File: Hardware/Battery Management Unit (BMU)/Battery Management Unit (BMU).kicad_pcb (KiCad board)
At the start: 4 copper layers, 105 x 65.5 mm, 93 parts, among them IC1 STM32C092RCT6, J1 HIGH SIDE, J10 SHUNT, J11 ALERT, J12 CAN, J13 Conn_ST_STDC14, J2 LOW SIDE, J3 POWER, J4 GPIO, J5 GND, J6 5V, J7 3V3, J8 FAULT, J9 I2C, Q1 DMP3099L, SW1 Power Switch, SW2 RESET Switch, T1 CEP99-102, T2 CEP99-102, U1 OKI-78SR-5_1.5-W36-C, U2 TLV75533PDBV, U3 PESD5V0L2BT, U4 BQ79600PWRQ1, U5 PESD5V0L2BT, U6 MCP2562FDT-H_SN

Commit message: Both boards are now fully completed: the BMU and CMU.
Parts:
- moved TP8 0.56 mm to (170.5, 87.8)
- moved TP14 0.28 mm to (151.5, 130.8)
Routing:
- net /BMU-COM Bridge/MISO/TX: track 29.9 -> 30.8 mm
- net /BMU-MCU/ALERT_SHUNT: track 49.3 -> 50.1 mm
- net /BMU-COM Bridge/FAULT_N: track 30.3 -> 29.6 mm
- net Net-(U4-BAT): track 16.2 -> 16.8 mm
- net /J4_CANL: track 24.7 -> 25.3 mm
- net /BMU-COM Bridge/MOSI/RX: track 37.4 -> 38.0 mm
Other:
- board text added: "VIKING MOTOR SPORTS (VMS) Battery Management Unit (BMU) 2026.4 Capstone TEAM-12"
- board text removed: "VIKING MOTOR SPORTS (VMS) BATTERY MANAGEMENT UNIT (BMU) 2026.4 Capstone TEAM-12"

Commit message: update layout
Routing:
- net +5V: vias 5 -> 4
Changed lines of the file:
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@@
-	)
-	(via
-		(at 171.5 102.5)
-		(size 0.6)
-		(drill 0.3)
-		(layers "F.Cu" "B.Cu")
-		(net "+5V")
 	)
 	(via

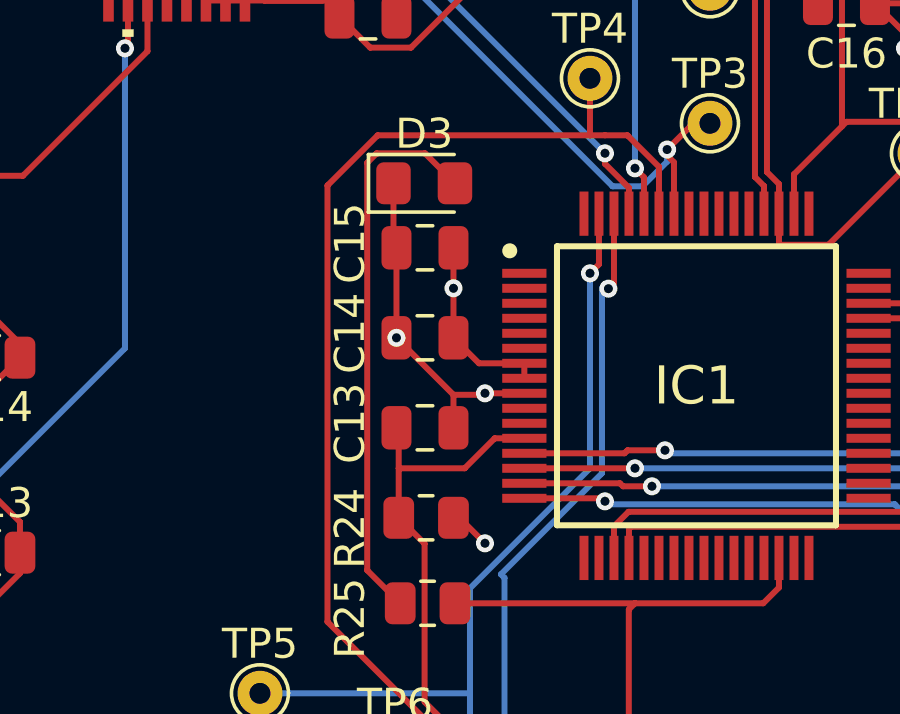
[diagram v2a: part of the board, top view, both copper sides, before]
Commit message: A bit of layout polish and bring in the correct stackup and DRUs from OSH Park
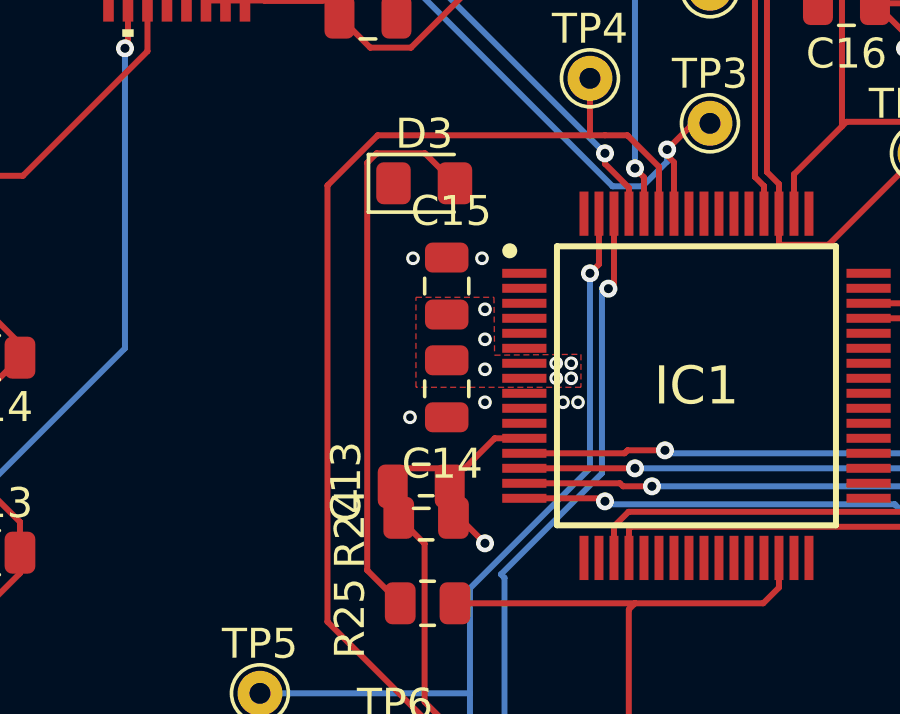
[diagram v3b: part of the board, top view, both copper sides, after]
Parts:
- moved C13 1.95 mm to (159.4, 119.6)
- moved C14 1.85 mm to (160.2, 116.3), turned to -90 degrees
- moved C15 1.47 mm to (160.2, 112.9), turned to 90 degrees
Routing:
- net GND: track 121.3 -> 109.9 mm, vias 14 -> 18
- net +3V3: track 42.0 -> 35.8 mm, vias 7 -> 13
- net Net-(IC1-PF2-NRST): track 54.9 -> 53.5 mm
- added copper zone on F.Cu, net +3V3

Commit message: update libraries+bmu
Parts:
- removed the J11 at (172.0, 131.5)
- removed the J9 at (161.0, 131.5)
- removed the R27 at (177.2, 95.4)
- removed the TP10 at (181.5, 108.5)
- removed the TP11 at (176.0, 108.5)
- removed TP17, TP18: TestPoint_Small, TestPoint:TestPoint_THTPad_D1.5mm_Drill0.7mm
- removed the TP4 at (165.0, 106.0)
- removed the TP7 at (185.5, 108.0)
- removed the TP8 at (170.5, 87.8)
- removed the TP9 at (170.5, 93.0)
- added R25: 10k, Resistor_SMD:R_0805_2012Metric, F.Cu at (173.0, 103.5)
- added R28: 1k, Resistor_SMD:R_0805_2012Metric, F.Cu at (183.0, 124.0)
- added TP12: TestPoint_Small, TestPoint:TestPoint_THTPad_D1.5mm_Drill0.7mm, F.Cu at (172.5, 108.0)
- added TP13: TestPoint_Small, TestPoint:TestPoint_THTPad_D1.5mm_Drill0.7mm, F.Cu at (176.5, 108.0)
- added TP14: TestPoint_Small, TestPoint:TestPoint_THTPad_D1.5mm_Drill0.7mm, F.Cu at (169.0, 103.5)
- added TP15: TestPoint_Small, TestPoint:TestPoint_THTPad_D1.5mm_Drill0.7mm, F.Cu at (181.0, 108.0)
- added TP16: TestPoint_Small, TestPoint:TestPoint_THTPad_D1.5mm_Drill0.7mm, F.Cu at (185.5, 108.0)
- added TP6: TestPoint_Small, TestPoint:TestPoint_THTPad_D1.5mm_Drill0.7mm, F.Cu at (182.0, 131.0)
- C1, C2: value 1u -> 10u
- CR1: footprint MMSZ5245B-7-F:SOD123_DIO -> Footprints:SOD123_DIO
- CR2: footprint ESDCAN03-2BWY:SOT323-3L_STM -> Footprints:SOT323-3L_STM
- IC1: footprint STM32C092RCT6:QFP50P1200X1200X160-64N -> Footprints:QFP50P1200X1200X160-64N
- J1, J2: footprint 705510038:CONN_70551-xxxx_04_MOL -> Footprints:705510038
- J10: footprint Connector_PinHeader_2.54mm:PinHeader_1x02_P2.54mm_Vertical -> Connector_PinHeader_2.54mm:PinHeader_1x05_P2.54mm_Vertical
- J4: footprint Connector_PinHeader_2.54mm:PinHeader_1x04_P2.54mm_Vertical -> Connector_PinHeader_2.54mm:PinHeader_1x05_P2.54mm_Vertical
- J8: value FAULT -> pin header; footprint Connector_PinHeader_2.54mm:PinHeader_1x01_P2.54mm_Vertical -> Connector_PinHeader_2.54mm:PinHeader_1x02_P2.54mm_Vertical
- J9: renamed from J12; footprint 691382000003:691382000003 -> Footprints:691382000003
- R26: value 10k -> 120
- SW2: value RESET Switch -> SW_Push; footprint Button_Switch_SMD:SW_Push_1P1T_NO_CK_KMR2 -> Button_Switch_THT:SW_PUSH_6mm_H4.3mm
- T1, T2: footprint CEP99-102:CEP99102 -> Footprints:CEP99102
- U3, U5: footprint PESD5V0L2BT:SOT23_NEX -> Footprints:SOT23_NEX
- U4: footprint BQ79600:TSSOP16_PW_TEX -> Footprints:TSSOP16_PW_TEX
- U6: footprint MCP2562FDT-H_SN:SOIC127P600X175-8N -> Footprints:SOIC127P600X175-8N
- moved SW2 35.4 mm to (153.8, 106.8), turned to -90 degrees
- moved TP4 22.5 mm to (176.0, 131.0)
- moved TP5 20.7 mm to (179.0, 131.0)
- moved J8 20.3 mm to (186.0, 126.5), turned to 180 degrees
- moved J4 19.5 mm to (166.1, 134.5), turned to -90 degrees
- moved TP11 19.3 mm to (170.5, 131.0)
- moved J10 18.2 mm to (173.5, 134.5), turned to 90 degrees
- moved TP2 11.5 mm to (165.5, 93.5)
- moved C17 10.1 mm to (172.5, 94.5), turned to 90 degrees
- moved C16 9.47 mm to (176.5, 94.5), turned to -90 degrees
- moved C6 6.82 mm to (154.5, 93.0)
- moved C7 6.57 mm to (157.5, 92.5), turned to 90 degrees
- moved TP10 5.66 mm to (165.0, 99.0)
- moved R26 5.20 mm to (170.0, 99.0), turned to -90 degrees
- moved TP1 4.61 mm to (165.5, 90.0)
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- renumbered J13 to J11, J6 to J5, J7 to J6, J5 to J7, R9 to R10, R10 to R11, R25 to R27, R11 to R9, TP15 to TP10, TP16 to TP11, TP5 to TP4, TP6 to TP5, TP12 to TP7, TP13 to TP8, TP14 to TP9
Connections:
- net /BMU-CAN/CAN_RX renamed /BMU-MCU/CAN_RXD
- net /BMU-CAN/CAN_TX renamed /BMU-MCU/CAN_TXD
- CR2 pad 1: /J4_CANH -> /CANH
- CR2 pad 2: /J4_CANL -> /CANL
- IC1 pad 30: /BMU-MCU/FAULT_LED -> Net-(IC1-PB10)
- IC1 pad 52: /BMU-CAN/CAN_STBY -> /BMU-MCU/STDBY
- IC1 pad 59: /BMU-MCU/ALERT_SHUNT -> /ALERT_SHUNT
- IC1 pad 62: /SCL_STM32 -> /I2C_SCL
- IC1 pad 63: /SDA_STM32 -> /I2C_SDA
- J10 pad 1: GND -> +3V3
- J10 pad 2: +3V3 -> /I2C_SDA
- J11 pad 7: unconnected-(J13-GND-Pad7) -> GND
- J4 pad 1: /BMU-MCU/SHUTDOWN -> /BMU-MCU/GPIO_SPARE1
- J4 pad 2: /BMU-MCU/GPIO_SPARE3 -> /BMU-MCU/GPIO_SPARE2
- J4 pad 3: /BMU-MCU/GPIO_SPARE2 -> /BMU-MCU/GPIO_SPARE3
- J4 pad 4: /BMU-MCU/GPIO_SPARE1 -> /BMU-MCU/SHUTDOWN
- J8 pad 1: /BMU-MCU/FAULT_LED -> GND
- J9 pad 1: /J4_CANH -> /CANH
- J9 pad 2: /J4_CANL -> /CANL
- R26 pad 1: /BMU-CAN/CAN_STBY -> /CANL
- R26 pad 2: GND -> /CANH
- R27 pad 1: /BMU-MCU/FAULT_LED -> Net-(IC1-PB10)
- TP4 pad 1: /SDA_STM32 -> /I2C_SDA
- TP5 pad 1: /SCL_STM32 -> /I2C_SCL
- U6 pad 6: /J4_CANL -> /CANL
- U6 pad 7: /J4_CANH -> /CANH
- U6 pad 8: /BMU-CAN/CAN_STBY -> /BMU-MCU/STDBY
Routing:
- net GND: track 109.9 -> 23.4 mm, vias 18 -> 33
- net /BMU-MCU/ALERT_SHUNT: track 50.1 -> 0.00 mm
- net /J4_CANH: track 40.7 -> 0.00 mm
- net /CANH: track 0.00 -> 34.8 mm
- net /SCL_STM32: track 32.3 -> 0.00 mm, vias 1 -> 0
- net /ALERT_SHUNT: track 0.00 -> 30.4 mm, vias 0 -> 1
- net /SDA_STM32: track 29.8 -> 0.00 mm, vias 1 -> 0
- net /I2C_SCL: track 0.00 -> 29.6 mm, vias 0 -> 1
- net /CANL: track 0.00 -> 28.9 mm
- net /I2C_SDA: track 0.00 -> 28.4 mm, vias 0 -> 1
- net /BMU-CAN/CAN_STBY: track 25.9 -> 0.00 mm
- net /J4_CANL: track 25.3 -> 0.00 mm, vias 1 -> 0
- net Net-(IC1-PB10): track 0.00 -> 24.7 mm
- net Net-(IC1-PF2-NRST): track 53.5 -> 73.6 mm
- net /BMU-MCU/FAULT_LED: track 19.9 -> 3.38 mm
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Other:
- board size 105 x 65.5 mm -> 105 x 66 mm

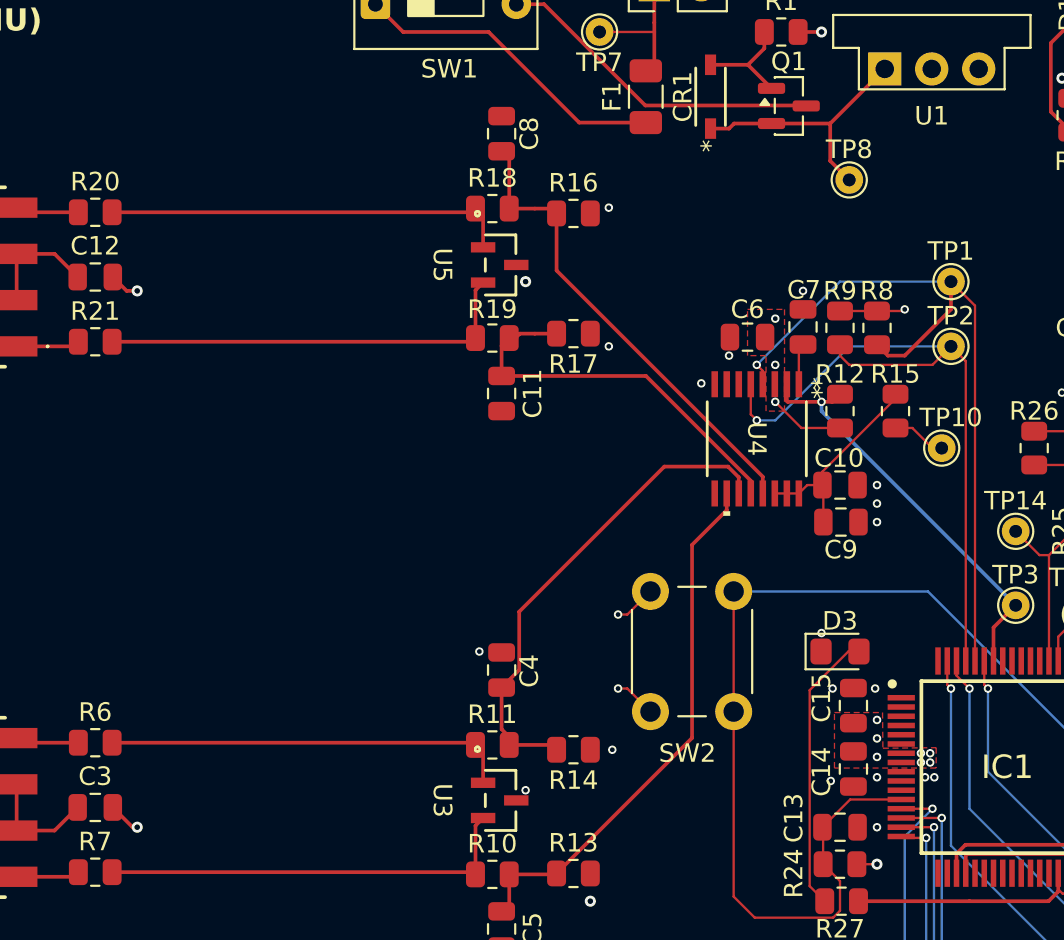
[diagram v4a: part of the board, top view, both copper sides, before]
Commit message: add via for bmu
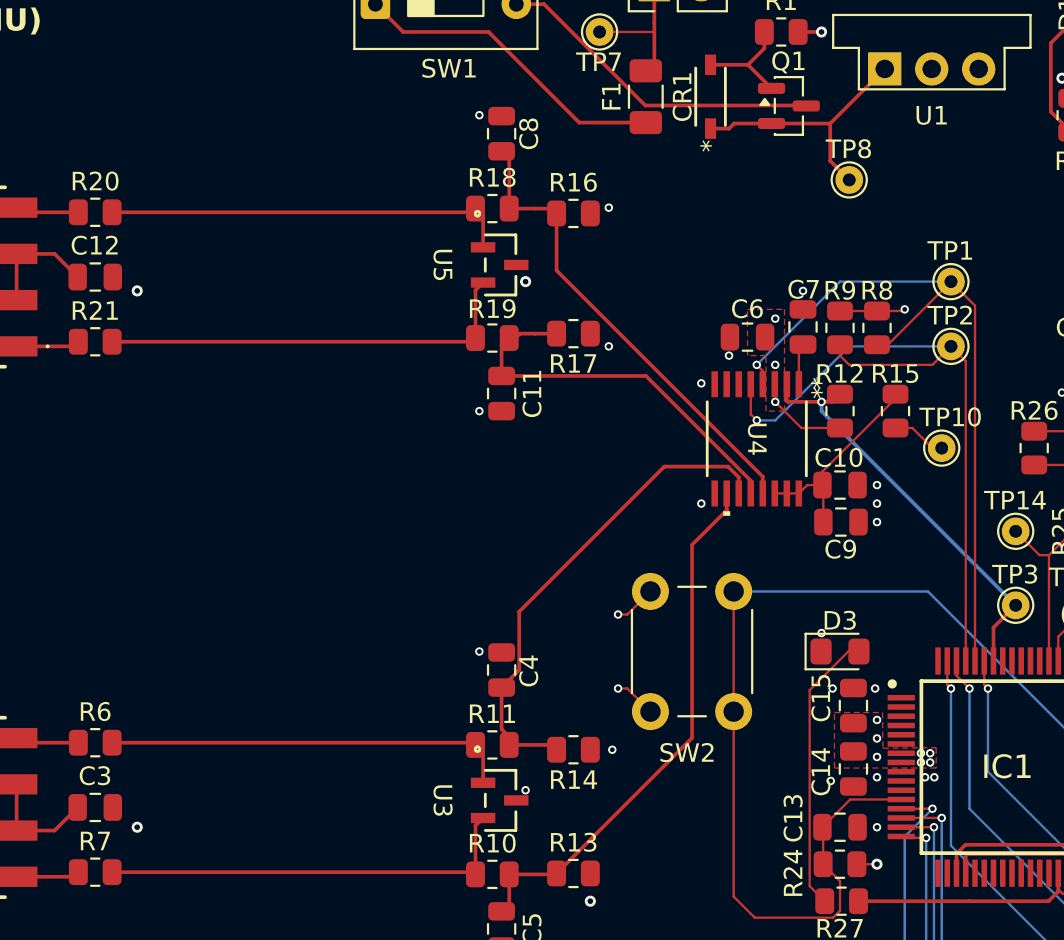
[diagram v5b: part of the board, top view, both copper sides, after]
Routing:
- net GND: track 23.4 -> 20.0 mm, vias 33 -> 36
- net /BMU-COM Bridge/MOSI/RX: track 41.4 -> 40.0 mm
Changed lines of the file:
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@@
-	)
-	(segment
-		(start 120.1802 118.4304)
-		(end 121.2498 119.5)
-		(width 0.2)
-		(layer "F.Cu")
-		(net "GND")
-	)
-	(segment
-		(start 120.9302 90.5)
-		(end 121.5 90.5)
-		(width 0.2)
-		(layer "F.Cu")
-		(net "GND")
 	)
 	(segment
@@
 	)
 	(segment
-		(start 121.2498 119.5)
-		(end 121.5 119.5)
-		(width 0.2)
-		(layer "F.Cu")
-		(net "GND")
-	)
-	(segment
 		(start 175.95 87)
 		(end 175.95 85.95)
@@
 		(start 141.812 97)
 		(end 141.20275 97)
-		(width 0.2)
-		(layer "F.Cu")
-		(net "GND")
-	)
-	(segment
-		(start 120.1802 89.75)
-		(end 120.9302 90.5)
 		(width 0.2)
 		(layer "F.Cu")
@@
 	)
 	(via
+		(at 140 97)
+		(size 0.4572)
+		(drill 0.254)
+		(layers "F.Cu" "B.Cu")
+		(free yes)
+		(net "GND")
+	)
+	(via
+		(at 140 81)
+		(size 0.4572)
+		(drill 0.254)
+		(layers "F.Cu" "B.Cu")
+		(free yes)
+		(net "GND")
+	)
+	(via
 		(at 161.5 119.5)
 		(size 0.4572)
@@
 	)
 	(via
+		(at 152 102)
+		(size 0.4572)
+		(drill 0.254)
+		(layers "F.Cu" "B.Cu")
+		(free yes)
+		(net "GND")
+	)
+	(via
 		(at 147.188 115.312)
 		(size 0.4572)
@@
 	)
 	(segment
-		(start 165.5 91.5)
-		(end 165.5 90)
-		(width 0.2)
-		(layer "F.Cu")
-		(net "/BMU-COM Bridge/MOSI{slash}RX")
-	)
-	(segment
 		(start 166.8 110.512)
 		(end 166.8 91.3)
@@
 	)
 	(segment
-		(start 163 94)
-		(end 165.5 91.5)
-		(width 0.2)
+		(start 165.5 90)
+		(end 162.0875 93.4125)
+		(width 0.127)
+		(layer "F.Cu")
+		(net "/BMU-COM Bridge/MOSI{slash}RX")
+	)
+	(segment
+		(start 162.0875 93.4125)
+		(end 161.5 93.4125)
+		(width 0.127)
 		(layer "F.Cu")
 		(net "/BMU-COM Bridge/MOSI{slash}RX")
@@
 	)
 	(segment
-		(start 163 94)
-		(end 162.0875 94)
-		(width 0.2)
-		(layer "F.Cu")
-		(net "/BMU-COM Bridge/MOSI{slash}RX")
-	)
-	(segment
 		(start 155.324993 94.824993)
 		(end 155.324993 95.54725)
@@
 		(layer "F.Cu")
 		(net "/BMU-COM Bridge/MOSI{slash}RX")
-	)
-	(segment
-		(start 162.0875 94)
-		(end 161.5 93.4125)
-		(width 0.2)
-		(layer "F.Cu")
-		(net "/BMU-COM Bridge/MOSI{slash}RX")

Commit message: Schematic cleanup; lots of missing library files
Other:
- board text added: "${TITLE} ${COMPANY} v${REVISION} ${ISSUE_DATE} Capstone TEAM-12"
- board text removed: "VIKING MOTOR SPORTS (VMS) Battery Management Unit (BMU) 2026.4 Capstone TEAM-12"
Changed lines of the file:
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@@
 	(title_block
 		(title "BATTERY MANAGEMENT UNIT (BMU)")
-		(date "2026-04-06")
-		(rev "1")
+		(date "2026-05-14")
+		(rev "1.0")
 		(company "VIKING MOTOR SPORTS (VMS)")
 	)
@@
 		(start 83.5 71)
 		(end 188.5 137)
+		(radius 1)
 		(stroke
 			(width 0.05)
-			(type default)
+			(type solid)
 		)
 		(fill no)
 		(layer "Edge.Cuts")
 	)
-	(gr_text "VIKING MOTOR SPORTS (VMS)\nBattery Management Unit (BMU)\n2026.4	Capstone TEAM-12\n"
-		(at 86 78.5 0)
+	(gr_text "${TITLE}\n${COMPANY}\nv${REVISION} ${ISSUE_DATE} \nCapstone TEAM-12\n"
+		(at 88.35 79.85 0)
 		(layer "F.SilkS")
 		(effects
